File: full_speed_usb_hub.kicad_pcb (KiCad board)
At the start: 2 copper layers, 100 x 30 mm, 39 parts, among them J1 USB_A, J2 USB_A, J3 USB_A, J4 USB_A, J5 USB_C_Receptacle_USB2.0_14P, U1 ADUM4160, U3 TLV73333PDBVR

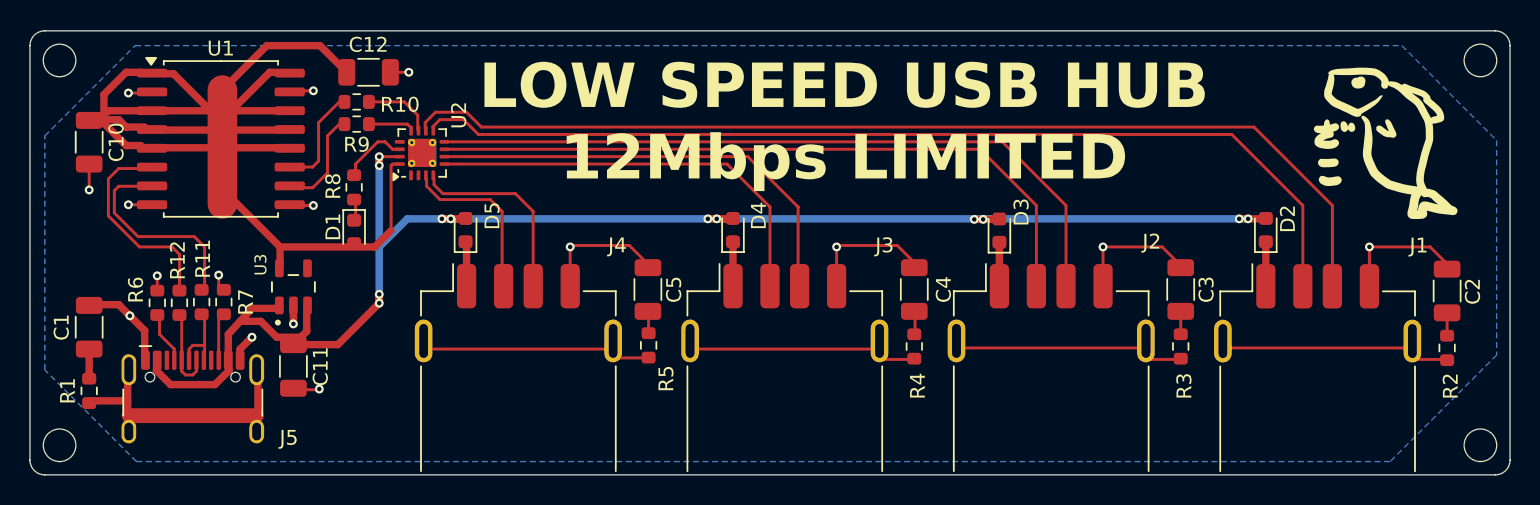
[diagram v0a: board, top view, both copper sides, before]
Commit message: update BOM and order PCBA
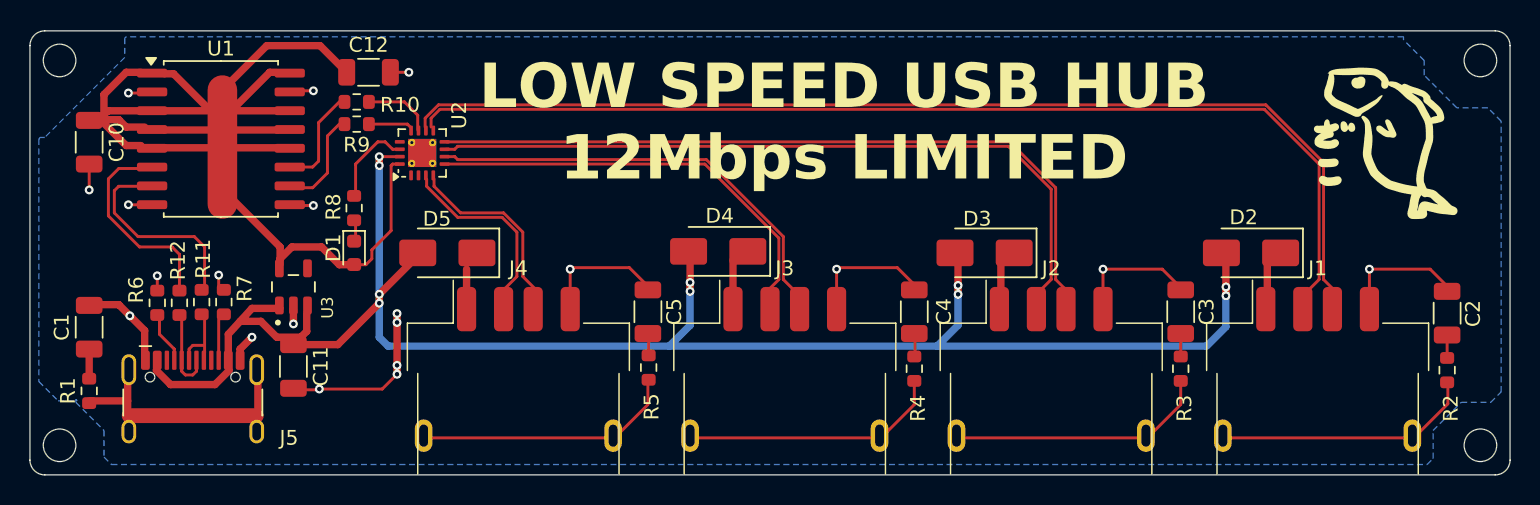
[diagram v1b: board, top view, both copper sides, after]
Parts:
- D2, D3, D4, D5: value D -> D SS34 C8678; footprint Diode_SMD:D_0603_1608Metric -> Diode_SMD:D_SMA
- J1, J2, J3, J4: value USB_A -> USB_A C668591; footprint Connector_USB:USB_A_Receptacle_GCT_USB1046 -> Library:USB_A_Receptacle_C668591
- R10, R11, R12, R9: value R 24 -> R 27
- U2: value ~ -> CH334P
- moved G*** 2.10 mm to (136.3, 113.0)
- moved D5 1.97 mm to (113.2, 115.0), turned to 180 degrees
- moved D2 1.83 mm to (167.5, 115.0), turned to 180 degrees
- moved D3 1.80 mm to (149.5, 115.0), turned to 180 degrees
- moved D4 1.75 mm to (131.5, 114.9), turned to 180 degrees
- moved J1 1.51 mm to (172.0, 123.0)
- moved C2 1.50 mm to (180.8, 119.1)
- moved C3 1.50 mm to (162.8, 119.0)
- moved C4 1.50 mm to (144.8, 119.0)
- moved C5 1.50 mm to (126.8, 119.0)
- moved J2 1.50 mm to (154.0, 123.0)
- moved J3 1.50 mm to (136.0, 123.0)
- moved J4 1.50 mm to (118.0, 123.0)
- moved R2 1.50 mm to (180.8, 122.9)
- moved R3 1.50 mm to (162.8, 122.8)
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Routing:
- net VBUS: vias 12 -> 10
- net GND: vias 16 -> 20
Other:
- board text added: "GND"
- board text added: "HOST PORT"
- board text added: "PORT 1"
- board text added: "PORT 2"
- board text added: "PORT 3"
- board text added: "PORT 4"
- board text added: "VBUS"
